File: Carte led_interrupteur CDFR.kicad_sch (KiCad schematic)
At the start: 16 parts, among them J1 Conn_01x10_Female, SW1 SW_Push, SW2 SW_Push, SW3 SW_DIP_x02

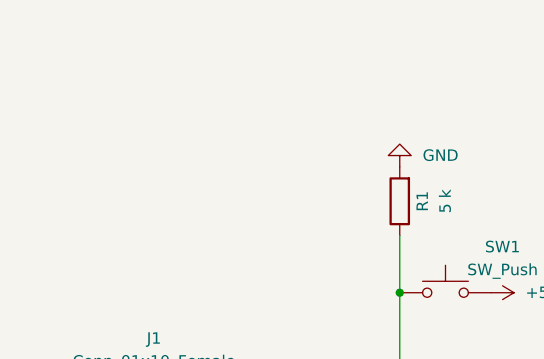
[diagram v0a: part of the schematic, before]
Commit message: change pin header
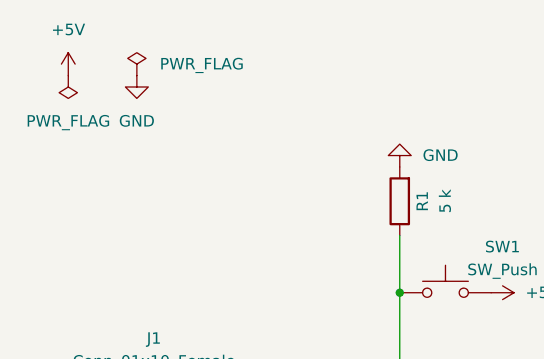
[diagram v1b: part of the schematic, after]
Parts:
- J1: footprint Connector_PinHeader_2.54mm:PinHeader_1x10_P2.54mm_Vertical -> Connector_PinHeader_2.54mm:PinHeader_2x05_P2.54mm_Vertical
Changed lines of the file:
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@@
     (pin "2")
+  )
+  (symbol (lib_id "power:+5V") (at 22.86 38.1 0) (unit 1)
+    (in_bom yes) (on_board yes) (fields_autoplaced)
+    (property "Reference" "#PWR0101" (id 0) (at 22.86 41.91 0)
+      (effects (font (size 1.27 1.27)) hide)
+    )
+    (property "Value" "+5V" (id 1) (at 22.86 33.02 0))
+    (property "Footprint" "" (id 2) (at 22.86 38.1 0)
+      (effects (font (size 1.27 1.27)) hide)
+    )
+    (property "Datasheet" "" (id 3) (at 22.86 38.1 0)
+      (effects (font (size 1.27 1.27)) hide)
+    )
+    (pin "1")
   )
   (symbol (lib_id "power:GND") (at 85.09 102.87 90) (unit 1)
@@
     (property "Reference" "J1" (id 0) (at 32.385 67.31 0))
     (property "Value" "Conn_01x10_Female" (id 1) (at 32.385 69.85 0))
-    (property "Footprint" "Connector_PinHeader_2.54mm:PinHeader_1x10_P2.54mm_Vertical" (id 2) (at 31.75 85.09 0)
+    (property "Footprint" "Connector_PinHeader_2.54mm:PinHeader_2x05_P2.54mm_Vertical" (id 2) (at 31.75 85.09 0)
       (effects (font (size 1.27 1.27)) hide)
     )
@@
     (pin "1")
   )
+  (symbol (lib_id "power:PWR_FLAG") (at 30.48 38.1 0) (unit 1)
+    (in_bom yes) (on_board yes) (fields_autoplaced)
+    (property "Reference" "#FLG0102" (id 0) (at 30.48 36.195 0)
+      (effects (font (size 1.27 1.27)) hide)
+    )
+    (property "Value" "PWR_FLAG" (id 1) (at 33.02 36.8299 0)
+      (effects (font (size 1.27 1.27)) (justify left))
+    )
+    (property "Footprint" "" (id 2) (at 30.48 38.1 0)
+      (effects (font (size 1.27 1.27)) hide)
+    )
+    (property "Datasheet" "~" (id 3) (at 30.48 38.1 0)
+      (effects (font (size 1.27 1.27)) hide)
+    )
+    (pin "1")
+  )
   (symbol (lib_id "power:+5V") (at 118.11 50.8 0) (unit 1)
     (in_bom yes) (on_board yes) (fields_autoplaced)
@@
     (pin "1")
   )
+  (symbol (lib_id "power:GND") (at 30.48 38.1 0) (unit 1)
+    (in_bom yes) (on_board yes) (fields_autoplaced)
+    (property "Reference" "#PWR0102" (id 0) (at 30.48 44.45 0)
+      (effects (font (size 1.27 1.27)) hide)
+    )
+    (property "Value" "GND" (id 1) (at 30.48 43.18 0))
+    (property "Footprint" "" (id 2) (at 30.48 38.1 0)
+      (effects (font (size 1.27 1.27)) hide)
+    )
+    (property "Datasheet" "" (id 3) (at 30.48 38.1 0)
+      (effects (font (size 1.27 1.27)) hide)
+    )
+    (pin "1")
+  )
   (symbol (lib_id "power:GND") (at 85.09 118.11 90) (unit 1)
     (in_bom yes) (on_board yes) (fields_autoplaced)
@@
     )
     (property "Datasheet" "" (id 3) (at 85.09 118.11 0)
+      (effects (font (size 1.27 1.27)) hide)
+    )
+    (pin "1")
+  )
+  (symbol (lib_id "power:PWR_FLAG") (at 22.86 38.1 180) (unit 1)
+    (in_bom yes) (on_board yes) (fields_autoplaced)
+    (property "Reference" "#FLG0101" (id 0) (at 22.86 40.005 0)
+      (effects (font (size 1.27 1.27)) hide)
+    )
+    (property "Value" "PWR_FLAG" (id 1) (at 22.86 43.18 0))
+    (property "Footprint" "" (id 2) (at 22.86 38.1 0)
+      (effects (font (size 1.27 1.27)) hide)
+    )
+    (property "Datasheet" "~" (id 3) (at 22.86 38.1 0)
       (effects (font (size 1.27 1.27)) hide)
     )
@@
   )
   (symbol_instances
+    (path "/d480d87c-bcd2-49e4-b15f-5ede46d52016"
+      (reference "#FLG0101") (unit 1) (value "PWR_FLAG") (footprint "")
+    )
+    (path "/a934f10e-3b88-4739-b98d-a9e0ad8d55ed"
+      (reference "#FLG0102") (unit 1) (value "PWR_FLAG") (footprint "")
+    )
     (path "/6809b97a-d5fc-471e-a859-b209bbc0714a"
       (reference "#PWR01") (unit 1) (value "GND") (footprint "")
@@
       (reference "#PWR013") (unit 1) (value "GND") (footprint "")
     )
+    (path "/7e0571ee-2bf3-4b86-95f6-412c70b00efa"
+      (reference "#PWR0101") (unit 1) (value "+5V") (footprint "")
+    )
+    (path "/c157dacc-0424-4736-8172-3d6cc404b369"
+      (reference "#PWR0102") (unit 1) (value "GND") (footprint "")
+    )
     (path "/5e6b3e5e-1038-43d3-9c66-dca427a87484"
       (reference "D1") (unit 1) (value "LED") (footprint "LED_THT:LED_D3.0mm")
@@
     )
     (path "/825a3efd-5cae-443a-b01f-e5d368b24ff8"
-      (reference "J1") (unit 1) (value "Conn_01x10_Female") (footprint "Connector_PinHeader_2.54mm:PinHeader_1x10_P2.54mm_Vertical")
+      (reference "J1") (unit 1) (value "Conn_01x10_Female") (footprint "Connector_PinHeader_2.54mm:PinHeader_2x05_P2.54mm_Vertical")
     )
     (path "/3bc7a19c-ada1-40ca-93c3-98fc697ce41c"
